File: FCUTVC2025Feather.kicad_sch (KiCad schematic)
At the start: 56 parts, among them J1 Micro_SD_Card_Det2, J2 Conn_01x03, J3 Conn_01x03, J4 Conn_01x02, J5 Conn_01x02, J6 Conn_01x02, J7 Conn_01x04, J8 Conn_01x02, J9 Conn_01x03, Q1 BSS138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

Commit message: finished pcb
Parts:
- removed C3: 10uF, Capacitor_SMD:C_0603_1608Metric, symbol Device:C
- removed C4: 2.7uF, Capacitor_SMD:C_0603_1608Metric, symbol Device:C
- removed J9: Conn_01x03, Connector_PinHeader_2.54mm:PinHeader_1x03_P2.54mm_Vertical, symbol Connector_Generic:Conn_01x03
- removed PS1: APXK004A0X-SRZ, FCU2025Lib:APXK004A0XSRZ, symbol APXK004A0X-SRZ:APXK004A0X-SRZ
- removed R1: 150R, Resistor_SMD:R_0402_1005Metric, symbol Device:R
- removed R2: 806R, Resistor_SMD:R_0402_1005Metric, symbol Device:R
- removed R3: 1k, Resistor_SMD:R_0402_1005Metric, symbol Device:R
- added J10, J11: Conn_01x04, Connector_PinHeader_2.54mm:PinHeader_1x04_P2.54mm_Vertical, symbol Connector_Generic:Conn_01x04
- added J12, J13: Conn_01x05, Connector_PinHeader_2.54mm:PinHeader_1x05_P2.54mm_Vertical, symbol Connector_Generic:Conn_01x05
- C19, C2, C22, C31: footprint Capacitor_SMD:C_0603_1608Metric -> Capacitor_SMD:C_0402_1005Metric
- J2, J3: footprint Connector_JST:JST_XH_S3B-XH-A_1x03_P2.50mm_Horizontal -> Connector_JST:JST_XH_B3B-XH-A_1x03_P2.50mm_Vertical
- J7: footprint Connector_JST:JST_PH_S4B-PH-K_1x04_P2.00mm_Horizontal -> Connector_JST:JST_PH_B4B-PH-K_1x04_P2.00mm_Vertical
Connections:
- net +3V3: now also J10.1 (Pin_1); no longer Q1.1 (G), Q2.1 (G), R4.2, R6.2
- net +6V/+8V: now also C1.1, C2.1, J5.1 (Pin_1), J6.1 (Pin_1), J8.1 (Pin_1), J13.1 (Pin_1)
- net GND: now also J10.4 (Pin_4), J11.4 (Pin_4); no longer U5.1 (S), U5.3 (S)
- net PYC1: now also J13.3 (Pin_3); no longer A1.9 (A4)
- net PYC2: now also J13.2 (Pin_2); no longer A1.10 (A5)
- net PYR1: now also J13.4 (Pin_4); no longer A1.21 (D2)
- net PYR2: now also J13.5 (Pin_5); no longer A1.22 (D3)
- net SRV1: now also J11.2 (Pin_2); no longer A1.19 (D0)
- net SRV2: now also J11.3 (Pin_3); no longer A1.20 (D1)
- net ARM: no longer names the net of J4.1 (Pin_1)
- net ARM: now also U5.1 (S), U5.3 (S)
- removed net VIN: C1.1, C19.1, C2.1, J5.1 (Pin_1), J6.1 (Pin_1), J8.1 (Pin_1), R21.1, U6.3 (VI)
- new net +3V3B: J11.1 (Pin_1), Q1.1 (G), Q2.1 (G), R4.2, R6.2
- new net PYC1A: A1.9 (A4), J12.2 (Pin_2)
- new net PYC2A: A1.10 (A5), J12.3 (Pin_3)
- new net PYR1A: A1.21 (D2), J12.4 (Pin_4)
- new net PYR2A: A1.22 (D3), J12.5 (Pin_5)
- new net SRV1A: A1.19 (D0), J10.2 (Pin_2)
- new net SRV2A: A1.20 (D1), J10.3 (Pin_3)
- new net VINA: C19.1, J12.1 (Pin_1), R21.1, U6.3 (VI)
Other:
- moved on the sheet: J4, J5, J7

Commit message: changed servo and pyro headers to JST XH (w/ hole). V1 complete
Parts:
- J2, J3: footprint Connector_JST:JST_XH_B3B-XH-A_1x03_P2.50mm_Vertical -> Connector_JST:JST_XH_B3B-XH-AM_1x03_P2.50mm_Vertical
- J4, J6, J8: footprint Connector_PinHeader_2.54mm:PinHeader_1x02_P2.54mm_Vertical -> Connector_JST:JST_XH_B2B-XH-AM_1x02_P2.50mm_Vertical
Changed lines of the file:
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@@
 			)
 		)
-		(property "Footprint" "Connector_JST:JST_XH_B3B-XH-A_1x03_P2.50mm_Vertical"
+		(property "Footprint" "Connector_JST:JST_XH_B3B-XH-AM_1x03_P2.50mm_Vertical"
 			(at 335.28 123.19 0)
 			(effects
@@
 			)
 		)
-		(property "Footprint" "Connector_PinHeader_2.54mm:PinHeader_1x02_P2.54mm_Vertical"
+		(property "Footprint" "Connector_JST:JST_XH_B2B-XH-AM_1x02_P2.50mm_Vertical"
 			(at 294.64 133.35 0)
 			(effects
@@
 			)
 		)
-		(property "Footprint" "Connector_PinHeader_2.54mm:PinHeader_1x02_P2.54mm_Vertical"
+		(property "Footprint" "Connector_JST:JST_XH_B2B-XH-AM_1x02_P2.50mm_Vertical"
 			(at 219.71 152.4 0)
 			(effects
@@
 			)
 		)
-		(property "Footprint" "Connector_PinHeader_2.54mm:PinHeader_1x02_P2.54mm_Vertical"
+		(property "Footprint" "Connector_JST:JST_XH_B2B-XH-AM_1x02_P2.50mm_Vertical"
 			(at 294.64 120.65 0)
 			(effects
@@
 			)
 		)
-		(property "Footprint" "Connector_JST:JST_XH_B3B-XH-A_1x03_P2.50mm_Vertical"
+		(property "Footprint" "Connector_JST:JST_XH_B3B-XH-AM_1x03_P2.50mm_Vertical"
 			(at 335.28 142.24 0)
 			(effects

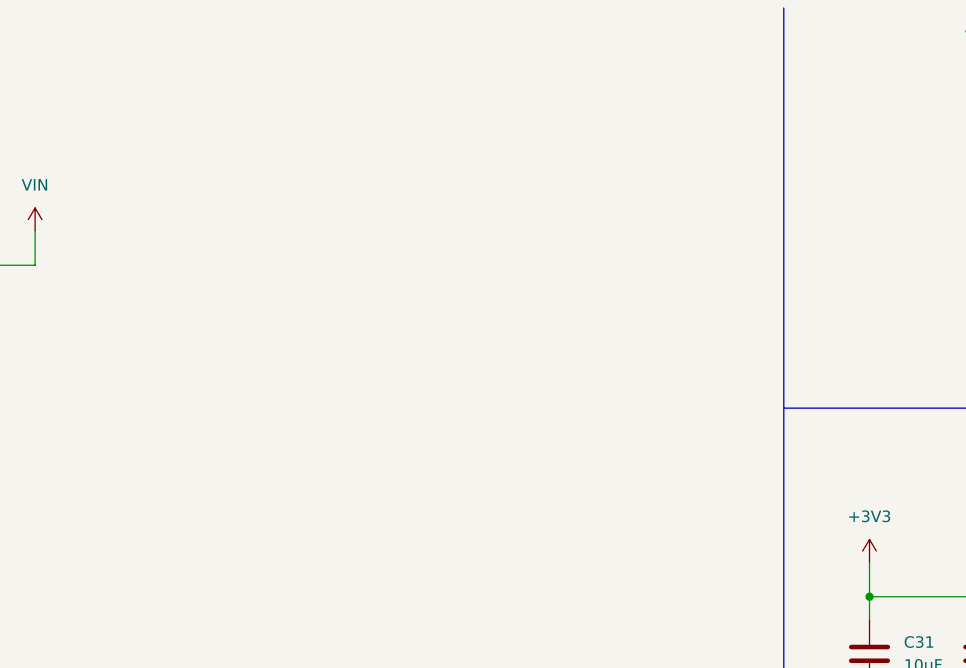
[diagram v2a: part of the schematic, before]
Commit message: added mounting holes (25mm 0 degrees, 150 degrees, 210 degrees)
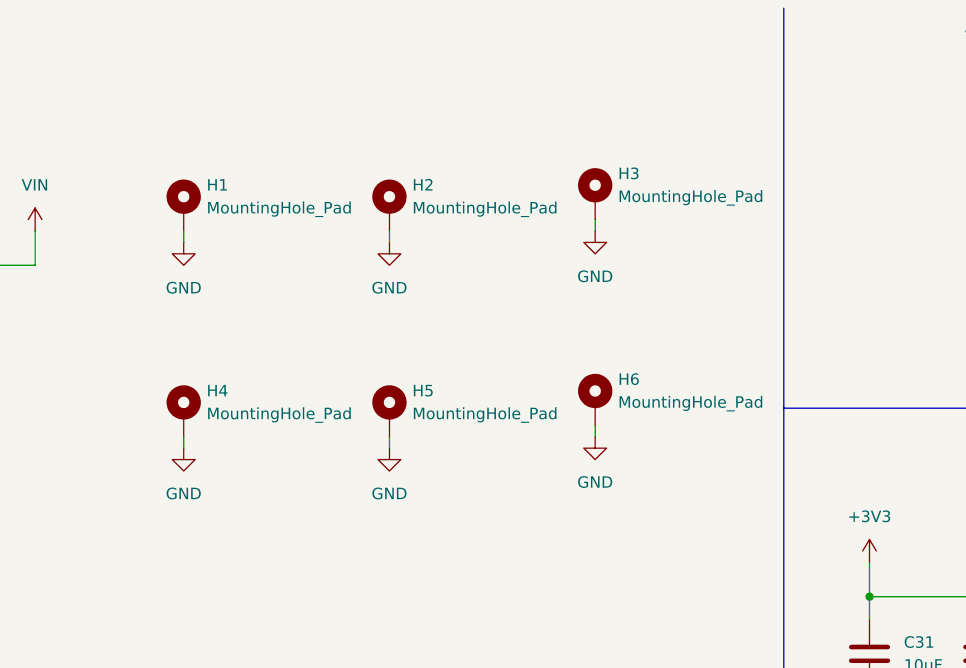
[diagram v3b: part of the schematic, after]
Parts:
- added H1, H2, H3, H4, H5, H6: MountingHole_Pad, MountingHole:MountingHole_4.3mm_M4_DIN965_Pad_TopBottom, symbol Mechanical:MountingHole_Pad
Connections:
- net GND: now also H1.1, H2.1, H3.1, H4.1, H5.1, H6.1
